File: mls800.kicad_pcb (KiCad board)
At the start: 2 copper layers, 293.4 x 80.5 mm, 106 parts, among them CON1 BARREL_JACK, IC1 6N137, J1 USB, J10 NSJ8HC, J11 NRJ4HF-1, J2 NRJ4HF-1, J3 NSJ8HC, J4 NSJ8HC, J5 NSJ8HC, J6 NSJ8HC, J7 NSJ8HC, J8 NSJ8HC, J9 NSJ8HC, P1 CONN_02X03, P2 DIN_5, P3 DIN_5, P4 CONN_02X03, P5 CONN_02X03, SW10 SW_TACT_LED, SW11 SW_TACT_LED, SW12 SW_PUSH_RIGHT_ANGLE, SW2 SW_TACT_LED, SW3 SW_TACT_LED, SW4 SW_TACT_LED, SW5 SW_TACT_LED, SW6 SW_TACT_LED, SW7 SW_TACT_LED, SW8 SW_TACT_LED, SW9 SW_TACT_LED, U1 LM340MP-5.0/NOPB, U2 ATmega32U4-AU, U3 24LC256, U4 MCP23017, U5 AS1115, U6 ULN2803A, U7 ULN2803A, U8 LM340MP-5.0/NOPB, X1 16Mhz

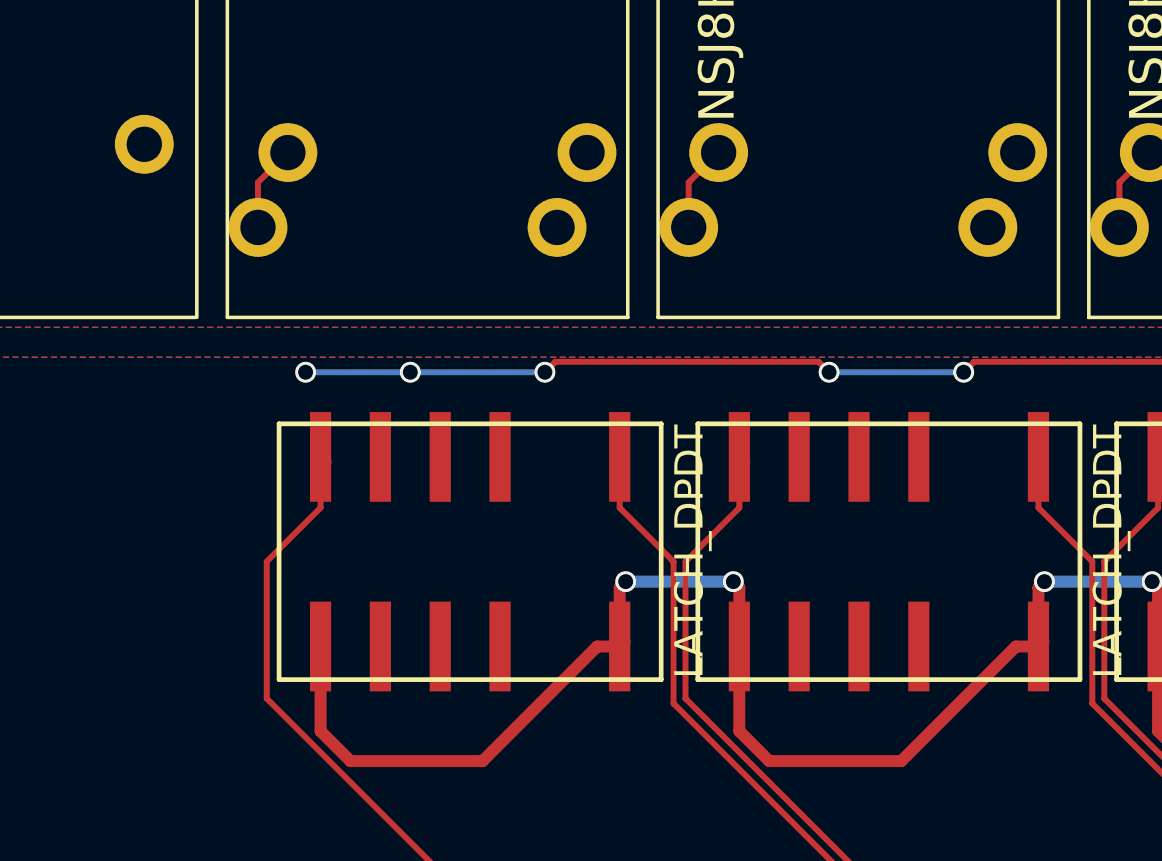
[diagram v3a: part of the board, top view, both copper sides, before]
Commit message: Found an acceptable routing pattern Started audio jacks routing.
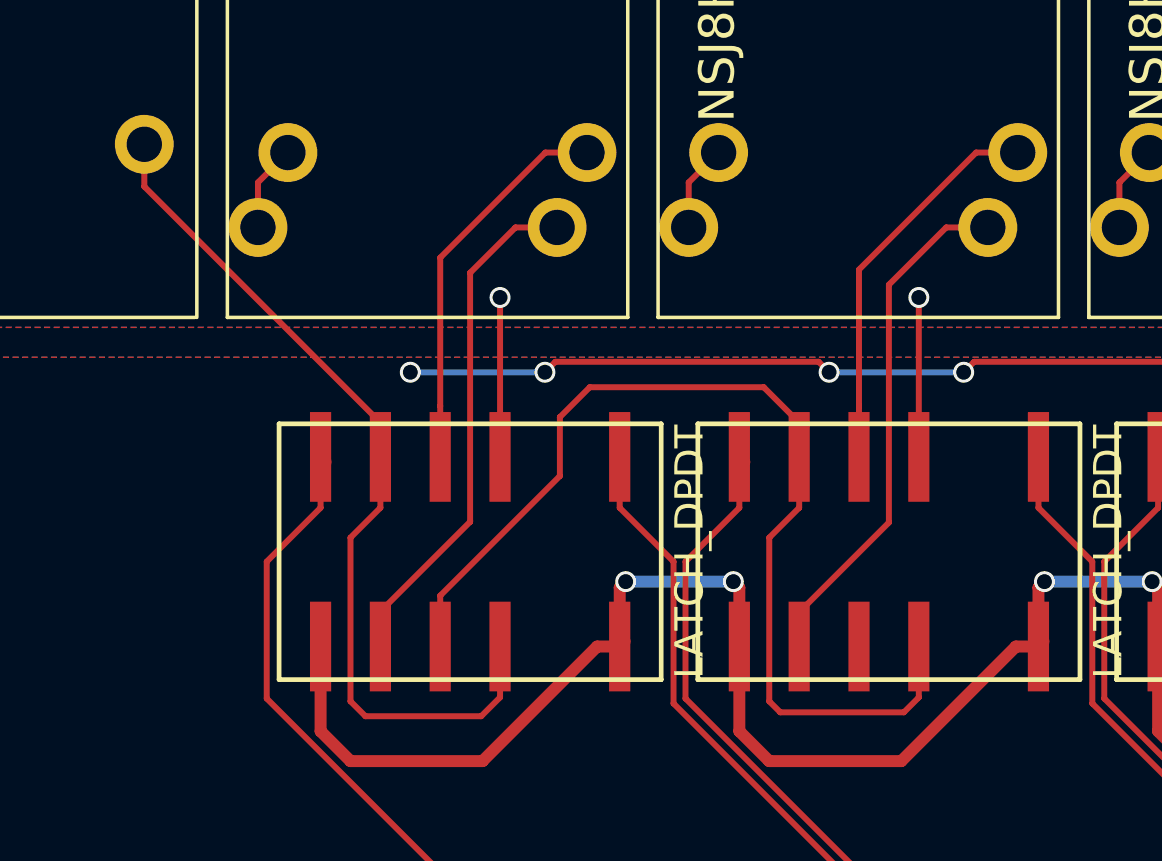
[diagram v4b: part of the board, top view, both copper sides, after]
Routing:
- net Net-(RE1-Pad9): track 0.00 -> 44.5 mm
- net Net-(J2-Pad1): track 0.00 -> 37.4 mm
- net Net-(J4-Pad5): track 1.45 -> 22.1 mm
- net Net-(J3-Pad5): track 1.45 -> 21.9 mm
- net Net-(J4-Pad6): track 0.00 -> 16.8 mm
- net Net-(J3-Pad6): track 0.00 -> 16.5 mm
- net GNDA: track 4.36 -> 17.9 mm, vias 0 -> 2
- net GND: track 195.6 -> 191.1 mm, vias 23 -> 22
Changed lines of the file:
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@@
   (general
     (links 345)
-    (no_connects 60)
+    (no_connects 55)
     (area 29.159999 45.161999 322.630001 125.780001)
     (thickness 1.6)
     (drawings 31)
-    (tracks 1100)
+    (tracks 1142)
     (zones 0)
     (modules 106)
@@
   (segment (start 161.099499 71.945501) (end 160.655 72.39) (width 0.254) (layer F.Cu) (net 15))
   (via (at 160.655 72.39) (size 0.889) (drill 0.635) (layers F.Cu B.Cu) (net 15))
-  (segment (start 66.04 72.39) (end 61.595 72.39) (width 0.254) (layer B.Cu) (net 15))
-  (via (at 61.595 72.39) (size 0.889) (drill 0.635) (layers F.Cu B.Cu) (net 15))
   (segment (start 71.755 72.39) (end 66.04 72.39) (width 0.254) (layer B.Cu) (net 15))
   (via (at 66.04 72.39) (size 0.889) (drill 0.635) (layers F.Cu B.Cu) (net 15))
@@
   (segment (start 294.990575 61.849009) (end 292.948367 61.849009) (width 0.254) (layer F.Cu) (net 29))
   (segment (start 295.91 62.768434) (end 294.990575 61.849009) (width 0.254) (layer F.Cu) (net 29))
+  (segment (start 54.746 62.712) (end 54.746 64.506) (width 0.254) (layer F.Cu) (net 30))
+  (segment (start 54.746 64.506) (end 64.77 74.53) (width 0.254) (layer F.Cu) (net 30))
+  (segment (start 64.77 74.53) (end 64.77 75.985) (width 0.254) (layer F.Cu) (net 30))
+  (segment (start 69.85 84.035) (end 69.85 86.194) (width 0.254) (layer F.Cu) (net 30))
+  (segment (start 69.85 86.194) (end 69.049 86.995) (width 0.254) (layer F.Cu) (net 30))
+  (segment (start 69.049 86.995) (end 64.135 86.995) (width 0.254) (layer F.Cu) (net 30))
+  (segment (start 64.135 86.995) (end 63.5 86.36) (width 0.254) (layer F.Cu) (net 30))
+  (segment (start 63.5 86.36) (end 63.5 79.414) (width 0.254) (layer F.Cu) (net 30))
+  (segment (start 63.5 79.414) (end 64.77 78.144) (width 0.254) (layer F.Cu) (net 30))
+  (segment (start 64.77 78.144) (end 64.77 75.985) (width 0.254) (layer F.Cu) (net 30))
   (segment (start 59.572 66.242) (end 59.572 64.332) (width 0.254) (layer F.Cu) (net 31))
   (segment (start 59.572 64.332) (end 60.842 63.062) (width 0.254) (layer F.Cu) (net 31))
-  (segment (start 64.77 84.035) (end 64.77 82.58) (width 0.254) (layer F.Cu) (net 32))
+  (segment (start 72.272 66.242) (end 70.504234 66.242) (width 0.254) (layer F.Cu) (net 32))
+  (segment (start 70.504234 66.242) (end 68.58 68.166234) (width 0.254) (layer F.Cu) (net 32))
+  (segment (start 68.58 68.166234) (end 68.58 78.74) (width 0.254) (layer F.Cu) (net 32))
+  (segment (start 68.58 78.74) (end 64.77 82.55) (width 0.254) (layer F.Cu) (net 32))
+  (segment (start 64.77 82.55) (end 64.77 84.035) (width 0.254) (layer F.Cu) (net 32))
+  (segment (start 73.542 63.062) (end 71.774234 63.062) (width 0.254) (layer F.Cu) (net 33))
+  (segment (start 71.774234 63.062) (end 67.31 67.526234) (width 0.254) (layer F.Cu) (net 33))
+  (segment (start 67.31 67.526234) (end 67.31 73.826) (width 0.254) (layer F.Cu) (net 33))
+  (segment (start 67.31 73.826) (end 67.31 75.985) (width 0.254) (layer F.Cu) (net 33))
   (segment (start 77.86 66.242) (end 77.86 64.332) (width 0.254) (layer F.Cu) (net 34))
   (segment (start 77.86 64.332) (end 79.13 63.062) (width 0.254) (layer F.Cu) (net 34))
-  (segment (start 82.55 84.035) (end 82.55 82.58) (width 0.254) (layer F.Cu) (net 35))
+  (segment (start 90.56 66.242) (end 88.792234 66.242) (width 0.254) (layer F.Cu) (net 35))
+  (segment (start 88.792234 66.242) (end 86.36 68.674234) (width 0.254) (layer F.Cu) (net 35))
+  (segment (start 86.36 68.674234) (end 86.36 78.77) (width 0.254) (layer F.Cu) (net 35))
+  (segment (start 86.36 78.77) (end 82.55 82.58) (width 0.254) (layer F.Cu) (net 35))
+  (segment (start 82.55 82.58) (end 82.55 84.035) (width 0.254) (layer F.Cu) (net 35))
+  (segment (start 91.83 63.062) (end 90.062234 63.062) (width 0.254) (layer F.Cu) (net 36))
+  (segment (start 90.062234 63.062) (end 85.09 68.034234) (width 0.254) (layer F.Cu) (net 36))
+  (segment (start 85.09 68.034234) (end 85.09 73.826) (width 0.254) (layer F.Cu) (net 36))
+  (segment (start 85.09 73.826) (end 85.09 75.985) (width 0.254) (layer F.Cu) (net 36))
   (segment (start 284.29 78.12) (end 284.29 77.645) (width 0.254) (layer F.Cu) (net 38))
   (segment (start 284.29 77.645) (end 281.575 74.93) (width 0.254) (layer F.Cu) (net 38))
@@
   (segment (start 281.586 84.62) (end 280.035 86.171) (width 0.254) (layer F.Cu) (net 90))
   (segment (start 282.59 84.62) (end 281.586 84.62) (width 0.254) (layer F.Cu) (net 90))
+  (segment (start 87.63 75.985) (end 87.63 69.215) (width 0.254) (layer F.Cu) (net 91))
+  (via (at 87.63 69.215) (size 0.889) (drill 0.635) (layers F.Cu B.Cu) (net 91))
+  (segment (start 69.85 75.985) (end 69.85 69.215) (width 0.254) (layer F.Cu) (net 91))
+  (via (at 69.85 69.215) (size 0.889) (drill 0.635) (layers F.Cu B.Cu) (net 91))
   (segment (start 69.85 75.985) (end 69.85 74.53) (width 0.254) (layer F.Cu) (net 91))
   (segment (start 87.63 75.985) (end 87.63 74.53) (width 0.254) (layer F.Cu) (net 91))
@@
   (segment (start 228.62 86.38) (end 228.6 86.36) (width 0.508) (layer F.Cu) (net 117))
   (segment (start 230.505 86.38) (end 228.62 86.38) (width 0.508) (layer F.Cu) (net 117))
+  (segment (start 81.28 86.36) (end 81.28 79.414) (width 0.254) (layer F.Cu) (net 118))
+  (segment (start 81.28 79.414) (end 82.55 78.144) (width 0.254) (layer F.Cu) (net 118))
+  (segment (start 82.55 78.144) (end 82.55 75.985) (width 0.254) (layer F.Cu) (net 118))
+  (segment (start 81.749 86.829) (end 81.28 86.36) (width 0.254) (layer F.Cu) (net 118))
+  (segment (start 86.995 86.829) (end 81.749 86.829) (width 0.254) (layer F.Cu) (net 118))
+  (segment (start 87.63 84.035) (end 87.63 86.194) (width 0.254) (layer F.Cu) (net 118))
+  (segment (start 87.63 86.194) (end 86.995 86.829) (width 0.254) (layer F.Cu) (net 118))
+  (segment (start 67.31 84.035) (end 67.31 81.876) (width 0.254) (layer F.Cu) (net 118))
+  (segment (start 67.31 81.876) (end 72.39 76.796) (width 0.254) (layer F.Cu) (net 118))
+  (segment (start 72.39 76.796) (end 72.39 74.295) (width 0.254) (layer F.Cu) (net 118))
+  (segment (start 72.39 74.295) (end 73.66 73.025) (width 0.254) (layer F.Cu) (net 118))
+  (segment (start 73.66 73.025) (end 81.045 73.025) (width 0.254) (layer F.Cu) (net 118))
+  (segment (start 81.045 73.025) (end 82.55 74.53) (width 0.254) (layer F.Cu) (net 118))
+  (segment (start 82.55 74.53) (end 82.55 75.985) (width 0.254) (layer F.Cu) (net 118))
   (segment (start 118.11 75.985) (end 118.11 78.144) (width 0.254) (layer F.Cu) (net 120))
   (segment (start 118.11 78.144) (end 116.84 79.414) (width 0.254) (layer F.Cu) (net 120))
